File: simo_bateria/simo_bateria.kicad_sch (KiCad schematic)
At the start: 4 parts, among them J1 conector salida, U2 cargador_bateria, U3 conversor_dc

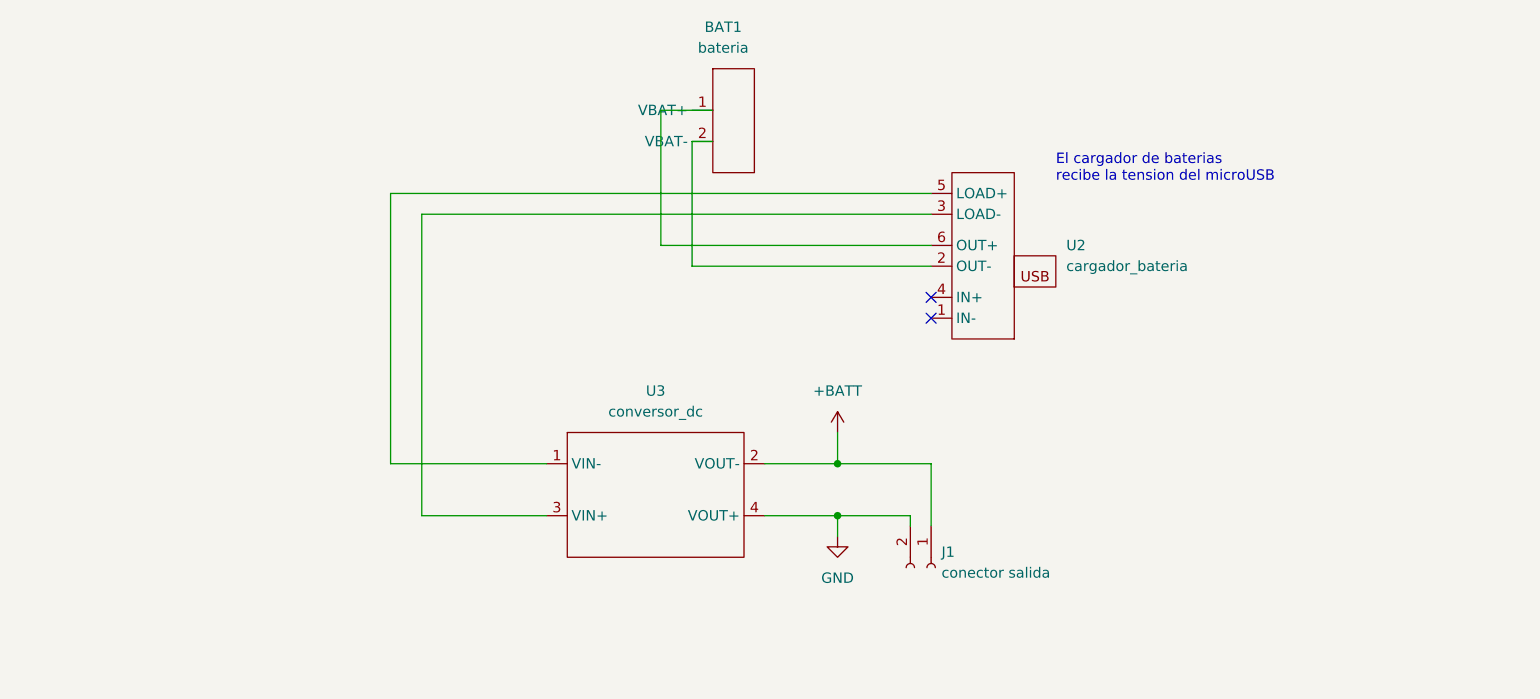
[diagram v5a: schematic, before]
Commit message: se agrego un circuito para mediciones de tension de bateria mediante la bluepill
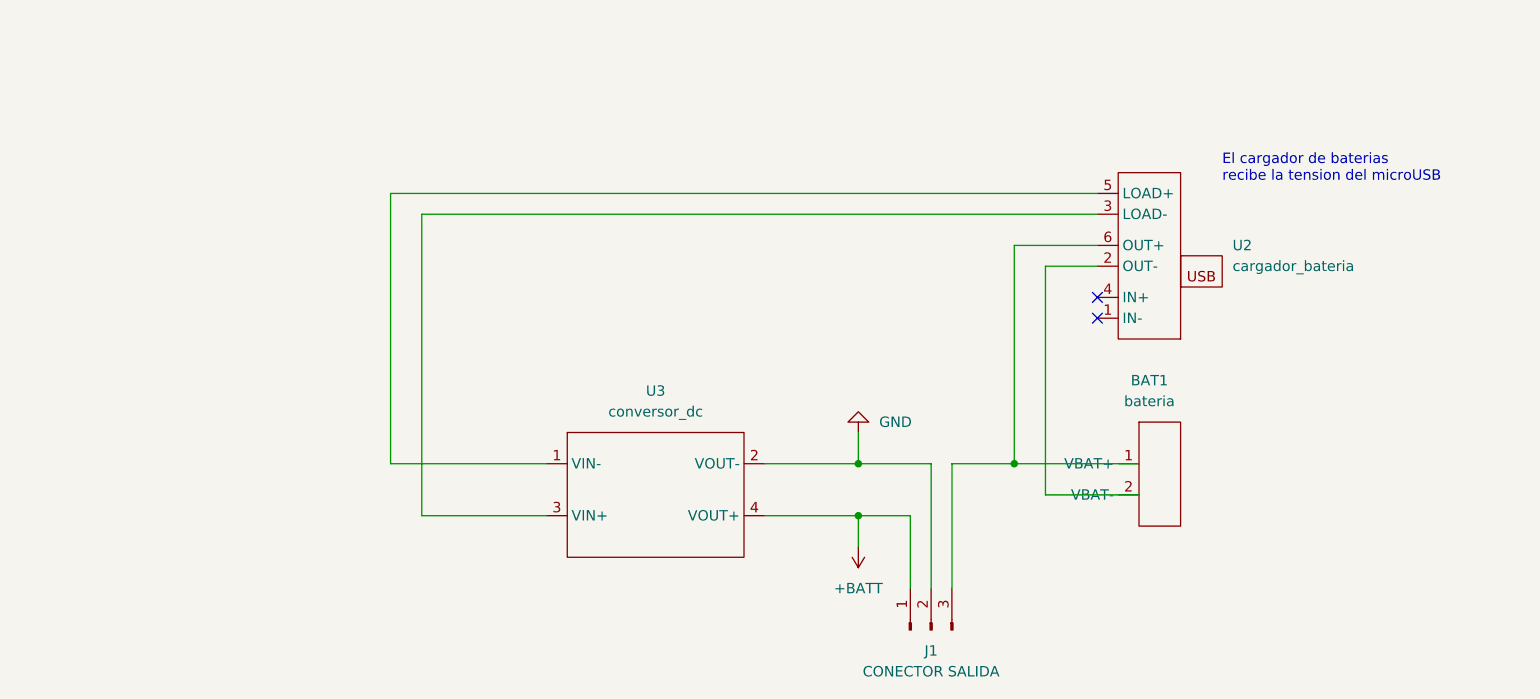
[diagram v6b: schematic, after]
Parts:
- removed J1: conector salida, Connector_JST:JST_EH_B2B-EH-A_1x02_P2.50mm_Vertical, symbol Connector:Conn_01x02_Female
- added J1: CONECTOR SALIDA, Connector_JST:JST_EH_B3B-EH-A_1x03_P2.50mm_Vertical, symbol Connector:Conn_01x03_Male
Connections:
- net +BATT: now also U3.4 (VOUT+), J1.1 (Pin_1); no longer U3.2 (VOUT-)
- net GND: now also U3.2 (VOUT-), J1.2 (Pin_2); no longer U3.4 (VOUT+)
- net at BAT1.1 (VBAT+), U2.6 (OUT+): now also J1.3 (Pin_3)
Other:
- moved on the sheet: BAT1, U2

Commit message: esquemas listos para revisar
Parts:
- removed J1: CONECTOR SALIDA, Connector_JST:JST_EH_B3B-EH-A_1x03_P2.50mm_Vertical, symbol Connector:Conn_01x03_Male
- removed U2: cargador_bateria, simo_bateria:cargador_bat, symbol simo_bateria:cargador_bateria
- added BAT2: bateria, Battery:BatteryHolder_MPD_BH-18650-PC2, symbol simo_bateria:bateria
- added J1: CONECTOR BATERIA( 8V), Connector_JST:JST_EH_B2B-EH-A_1x02_P2.50mm_Vertical, symbol Connector:Conn_01x02_Male
- added J2: CONECTOR PLUG IN (5V), Connector_JST:JST_EH_B2B-EH-A_1x02_P2.50mm_Vertical, symbol Connector:Conn_01x02_Male
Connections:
- net at BAT1.1 (VBAT+): now also BAT2.2 (VBAT-)
- net at BAT1.2 (VBAT-): now also U3.1 (VIN-), J1.2 (Pin_2)
- net at U3.3 (VIN+): now also BAT2.1 (VBAT+), J1.1 (Pin_1)
- net +BATT: no longer names the net of U3.4 (VOUT+)
- net +BATT: now also J2.2 (Pin_2)
- net GND: no longer names the net of U3.2 (VOUT-)
- net GND: now also J2.1 (Pin_1)
- no-connect marks 2 -> 0
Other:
- note removed: "El cargador de baterias recibe la tension del microUSB"
- moved on the sheet: U3

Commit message: update
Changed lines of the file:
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@@
 (kicad_sch (version 20211123) (generator eeschema)
   (paper "A4")
+  (junction (at 78.74 64.77) (diameter 0) (color 0 0 0 0)
+  )
   (junction (at 67.437 53.467) (diameter 0) (color 0 0 0 0)
   )
   (junction (at 64.897 72.898) (diameter 0) (color 0 0 0 0)
+  )
+  (junction (at 78.74 59.69) (diameter 0) (color 0 0 0 0)
   )
   (wire (pts (xy 67.437 33.655) (xy 67.437 53.467))
@@
     (stroke (width 0) (type default) (color 0 0 0 0))
   )
+  (wire (pts (xy 78.74 64.77) (xy 78.74 68.453))
+    (stroke (width 0) (type default) (color 0 0 0 0))
+  )
+  (wire (pts (xy 78.74 53.086) (xy 78.74 59.69))
+    (stroke (width 0) (type default) (color 0 0 0 0))
+  )
   (wire (pts (xy 67.437 53.467) (xy 75.692 53.467))
     (stroke (width 0) (type default) (color 0 0 0 0))
   )
-  (wire (pts (xy 75.692 59.69) (xy 82.042 59.69))
+  (wire (pts (xy 75.692 59.69) (xy 78.74 59.69))
     (stroke (width 0) (type default) (color 0 0 0 0))
   )
@@
   )
   (wire (pts (xy 64.897 33.655) (xy 64.897 72.898))
+    (stroke (width 0) (type default) (color 0 0 0 0))
+  )
+  (wire (pts (xy 78.74 64.77) (xy 82.042 64.77))
     (stroke (width 0) (type default) (color 0 0 0 0))
   )
@@
     (stroke (width 0) (type default) (color 0 0 0 0))
   )
+  (wire (pts (xy 78.74 59.69) (xy 82.042 59.69))
+    (stroke (width 0) (type default) (color 0 0 0 0))
+  )
   (wire (pts (xy 50.546 69.088) (xy 53.467 69.088))
     (stroke (width 0) (type default) (color 0 0 0 0))
@@
     (stroke (width 0) (type default) (color 0 0 0 0))
   )
-  (wire (pts (xy 75.565 64.77) (xy 82.042 64.77))
+  (wire (pts (xy 75.565 64.77) (xy 78.74 64.77))
     (stroke (width 0) (type default) (color 0 0 0 0))
   )
@@
     (pin "1")
     (pin "2")
+  )
+  (symbol (lib_id "power:PWR_FLAG") (at 78.74 53.086 0) (unit 1)
+    (in_bom yes) (on_board yes) (fields_autoplaced)
+    (property "Reference" "#FLG0101" (id 0) (at 78.74 51.181 0)
+      (effects (font (size 1.27 1.27)) hide)
+    )
+    (property "Value" "PWR_FLAG" (id 1) (at 78.74 48.26 0))
+    (property "Footprint" "" (id 2) (at 78.74 53.086 0)
+      (effects (font (size 1.27 1.27)) hide)
+    )
+    (property "Datasheet" "~" (id 3) (at 78.74 53.086 0)
+      (effects (font (size 1.27 1.27)) hide)
+    )
+    (pin "1")
+  )
+  (symbol (lib_id "power:PWR_FLAG") (at 78.74 68.453 180) (unit 1)
+    (in_bom yes) (on_board yes) (fields_autoplaced)
+    (property "Reference" "#FLG0102" (id 0) (at 78.74 70.358 0)
+      (effects (font (size 1.27 1.27)) hide)
+    )
+    (property "Value" "PWR_FLAG" (id 1) (at 80.645 69.7229 0)
+      (effects (font (size 1.27 1.27)) (justify right))
+    )
+    (property "Footprint" "" (id 2) (at 78.74 68.453 0)
+      (effects (font (size 1.27 1.27)) hide)
+    )
+    (property "Datasheet" "~" (id 3) (at 78.74 68.453 0)
+      (effects (font (size 1.27 1.27)) hide)
+    )
+    (pin "1")
   )
   (symbol (lib_id "simo_bateria:conversor_dc") (at 84.582 53.34 0) (unit 1)
@@
     (pin "2")
   )
-  (symbol (lib_id "simo_bateria:bateria") (at 45.466 62.357 180) (unit 1)
+  (symbol (lib_name "bateria_1") (lib_id "simo_bateria:bateria") (at 45.466 62.357 180) (unit 1)
     (in_bom yes) (on_board yes)
     (property "Reference" "BAT2" (id 0) (at 36.195 57.15 0))
@@
   )
   (symbol_instances
+    (path "/94a04b5b-32cd-4810-a8b4-c20fa7084dfb"
+      (reference "#FLG0101") (unit 1) (value "PWR_FLAG") (footprint "")
+    )
+    (path "/be968050-f6bb-4281-b884-b98d3ee6f6cc"
+      (reference "#FLG0102") (unit 1) (value "PWR_FLAG") (footprint "")
+    )
     (path "/7c976c15-6a2b-49f8-a800-ad9c7274e7f5"
       (reference "BAT1") (unit 1) (value "bateria") (footprint "Battery:BatteryHolder_MPD_BH-18650-PC2")
